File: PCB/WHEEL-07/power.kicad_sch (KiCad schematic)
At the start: 21 parts, among them IC2 LDO40LPU50RY, IC3 MP2332HGTL-P, Q1 AO3401A

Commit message: Changed connectors setup
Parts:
- C14: footprint Capacitor_SMD:C_0201_0603Metric -> Capacitor_SMD:C_0603_1608Metric
- C15, C21, C22: footprint Capacitor_SMD:C_0402_1005Metric -> Capacitor_SMD:C_0402_1005Metric_Pad0.74x0.62mm_HandSolder
- R10, R11, R19, R7, R8, R9: footprint Resistor_SMD:R_0402_1005Metric -> Resistor_SMD:R_0402_1005Metric_Pad0.72x0.64mm_HandSolder
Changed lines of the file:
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@@
     (property "Reference" "R9" (id 0) (at 204.47 57.785 90))
     (property "Value" "20k" (id 1) (at 204.47 55.88 90))
-    (property "Footprint" "Resistor_SMD:R_0402_1005Metric" (id 2) (at 204.47 53.34 0)
+    (property "Footprint" "Resistor_SMD:R_0402_1005Metric_Pad0.72x0.64mm_HandSolder" (id 2) (at 204.47 53.34 0)
       (effects (font (size 1.27 1.27)) hide)
     )
@@
       (effects (font (size 1.27 1.27)) (justify left))
     )
-    (property "Footprint" "Resistor_SMD:R_0402_1005Metric" (id 2) (at 48.26 118.745 0)
+    (property "Footprint" "Resistor_SMD:R_0402_1005Metric_Pad0.72x0.64mm_HandSolder" (id 2) (at 48.26 118.745 0)
       (effects (font (size 1.27 1.27)) hide)
     )
@@
     (property "Reference" "R8" (id 0) (at 203.2 39.37 90))
     (property "Value" "20" (id 1) (at 203.2 41.91 90))
-    (property "Footprint" "Resistor_SMD:R_0402_1005Metric" (id 2) (at 203.2 45.72 0)
+    (property "Footprint" "Resistor_SMD:R_0402_1005Metric_Pad0.72x0.64mm_HandSolder" (id 2) (at 203.2 45.72 0)
       (effects (font (size 1.27 1.27)) hide)
     )
@@
     (property "Reference" "R11" (id 0) (at 217.17 58.42 90))
     (property "Value" "40.2k" (id 1) (at 217.17 55.88 90))
-    (property "Footprint" "Resistor_SMD:R_0402_1005Metric" (id 2) (at 217.17 53.34 0)
+    (property "Footprint" "Resistor_SMD:R_0402_1005Metric_Pad0.72x0.64mm_HandSolder" (id 2) (at 217.17 53.34 0)
       (effects (font (size 1.27 1.27)) hide)
     )
@@
       (effects (font (size 1.27 1.27)) (justify left))
     )
-    (property "Footprint" "Capacitor_SMD:C_0402_1005Metric" (id 2) (at 227.965 45.085 0)
+    (property "Footprint" "Capacitor_SMD:C_0402_1005Metric_Pad0.74x0.62mm_HandSolder" (id 2) (at 227.965 45.085 0)
       (effects (font (size 1.27 1.27)) hide)
     )
@@
     (property "Reference" "R7" (id 0) (at 151.765 52.07 90))
     (property "Value" "200k" (id 1) (at 150.495 53.975 90))
-    (property "Footprint" "Resistor_SMD:R_0402_1005Metric" (id 2) (at 153.035 49.53 0)
+    (property "Footprint" "Resistor_SMD:R_0402_1005Metric_Pad0.72x0.64mm_HandSolder" (id 2) (at 153.035 49.53 0)
       (effects (font (size 1.27 1.27)) hide)
     )
@@
       (effects (font (size 1.27 1.27)) (justify left))
     )
-    (property "Footprint" "Resistor_SMD:R_0402_1005Metric" (id 2) (at 209.55 63.5 0)
+    (property "Footprint" "Resistor_SMD:R_0402_1005Metric_Pad0.72x0.64mm_HandSolder" (id 2) (at 209.55 63.5 0)
       (effects (font (size 1.27 1.27)) hide)
     )
@@
       (effects (font (size 1.27 1.27)) (justify left))
     )
-    (property "Footprint" "Capacitor_SMD:C_0402_1005Metric" (id 2) (at 237.49 45.085 0)
+    (property "Footprint" "Capacitor_SMD:C_0402_1005Metric_Pad0.74x0.62mm_HandSolder" (id 2) (at 237.49 45.085 0)
       (effects (font (size 1.27 1.27)) hide)
     )
@@
       (effects (font (size 1.27 1.27)) (justify left))
     )
-    (property "Footprint" "Capacitor_SMD:C_0201_0603Metric" (id 2) (at 80.645 46.355 0)
+    (property "Footprint" "Capacitor_SMD:C_0603_1608Metric" (id 2) (at 80.645 46.355 0)
       (effects (font (size 1.27 1.27)) hide)
     )
@@
       (effects (font (size 1.27 1.27)) (justify left))
     )
-    (property "Footprint" "Capacitor_SMD:C_0402_1005Metric" (id 2) (at 155.575 41.91 0)
-      (effects (font (size 1.27 1.27)) hide)
-    )
+    (property "Footprint" "Capacitor_SMD:C_0402_1005Metric_Pad0.74x0.62mm_HandSolder" (id 2) (at 155.575 41.91 0)
+      (effects (font (size 1.27 1.27)) hide)
+    )

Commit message: Finished layout
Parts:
- removed R19: 100, Resistor_SMD:R_0402_1005Metric_Pad0.72x0.64mm_HandSolder, symbol Device:R_Small
- C15: footprint Capacitor_SMD:C_0402_1005Metric_Pad0.74x0.62mm_HandSolder -> Capacitor_SMD:C_0805_2012Metric
- C16, C17, C18, C19, C20: footprint (none) -> Capacitor_SMD:C_0402_1005Metric_Pad0.74x0.62mm_HandSolder
- L2: footprint (none) -> Inductor_SMD:L_Vishay_IHLP-1616
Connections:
- net GND: now also Q1.1 (G)
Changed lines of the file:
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@@
   (junction (at 222.25 53.34) (diameter 0) (color 0 0 0 0)
+  )
+  (junction (at 65.405 107.315) (diameter 0) (color 0 0 0 0)
   )
   (junction (at 149.225 45.72) (diameter 0) (color 0 0 0 0)
@@
     (stroke (width 0) (type default) (color 0 0 0 0))
   )
-  (wire (pts (xy 48.26 121.285) (xy 48.26 122.555))
-    (stroke (width 0) (type default) (color 0 0 0 0))
-  )
   (wire (pts (xy 57.785 60.325) (xy 57.785 61.595))
     (stroke (width 0) (type default) (color 0 0 0 0))
@@
     (stroke (width 0) (type default) (color 0 0 0 0))
   )
-  (wire (pts (xy 64.135 107.315) (xy 66.04 107.315))
+  (wire (pts (xy 64.135 107.315) (xy 65.405 107.315))
     (stroke (width 0) (type default) (color 0 0 0 0))
   )
@@
     (stroke (width 0) (type default) (color 0 0 0 0))
   )
+  (wire (pts (xy 65.405 106.045) (xy 65.405 107.315))
+    (stroke (width 0) (type default) (color 0 0 0 0))
+  )
   (wire (pts (xy 237.49 49.53) (xy 240.665 49.53))
     (stroke (width 0) (type default) (color 0 0 0 0))
@@
   )
   (wire (pts (xy 170.18 59.69) (xy 172.085 59.69))
+    (stroke (width 0) (type default) (color 0 0 0 0))
+  )
+  (wire (pts (xy 65.405 107.315) (xy 66.04 107.315))
     (stroke (width 0) (type default) (color 0 0 0 0))
   )
@@
       (effects (font (size 1.27 1.27)) (justify left))
     )
-    (property "Footprint" "" (id 2) (at 166.116 41.91 0)
+    (property "Footprint" "Capacitor_SMD:C_0402_1005Metric_Pad0.74x0.62mm_HandSolder" (id 2) (at 166.116 41.91 0)
       (effects (font (size 1.27 1.27)) hide)
     )
@@
     (pin "2")
   )
-  (symbol (lib_id "Device:R_Small") (at 48.26 118.745 0) (unit 1)
-    (in_bom yes) (on_board yes) (fields_autoplaced)
-    (property "Reference" "R19" (id 0) (at 50.165 117.4749 0)
-      (effects (font (size 1.27 1.27)) (justify left))
-    )
-    (property "Value" "100" (id 1) (at 50.165 120.0149 0)
-      (effects (font (size 1.27 1.27)) (justify left))
-    )
-    (property "Footprint" "Resistor_SMD:R_0402_1005Metric_Pad0.72x0.64mm_HandSolder" (id 2) (at 48.26 118.745 0)
-      (effects (font (size 1.27 1.27)) hide)
-    )
-    (property "Datasheet" "~" (id 3) (at 48.26 118.745 0)
-      (effects (font (size 1.27 1.27)) hide)
-    )
-    (pin "1")
-    (pin "2")
-  )
   (symbol (lib_id "WHEEL_07:LDO40LPU50RY") (at 40.005 37.465 0) (unit 1)
     (in_bom yes) (on_board yes) (fields_autoplaced)
@@
     (pin "1")
   )
-  (symbol (lib_id "power:GND") (at 48.26 122.555 0) (unit 1)
-    (in_bom yes) (on_board yes) (fields_autoplaced)
-    (property "Reference" "#PWR0168" (id 0) (at 48.26 128.905 0)
-      (effects (font (size 1.27 1.27)) hide)
-    )
-    (property "Value" "GND" (id 1) (at 48.26 127 0))
-    (property "Footprint" "" (id 2) (at 48.26 122.555 0)
-      (effects (font (size 1.27 1.27)) hide)
-    )
-    (property "Datasheet" "" (id 3) (at 48.26 122.555 0)
+  (symbol (lib_id "power:GND") (at 48.26 116.205 0) (unit 1)
+    (in_bom yes) (on_board yes) (fields_autoplaced)
+    (property "Reference" "#PWR0168" (id 0) (at 48.26 122.555 0)
+      (effects (font (size 1.27 1.27)) hide)
+    )
+    (property "Value" "GND" (id 1) (at 48.26 120.65 0))
+    (property "Footprint" "" (id 2) (at 48.26 116.205 0)
+      (effects (font (size 1.27 1.27)) hide)
+    )
+    (property "Datasheet" "" (id 3) (at 48.26 116.205 0)
       (effects (font (size 1.27 1.27)) hide)
     )
@@
     (property "Reference" "C20" (id 0) (at 217.17 67.945 90))
     (property "Value" "10pF" (id 1) (at 217.17 69.85 90))
-    (property "Footprint" "" (id 2) (at 217.17 64.77 0)
+    (property "Footprint" "Capacitor_SMD:C_0402_1005Metric_Pad0.74x0.62mm_HandSolder" (id 2) (at 217.17 64.77 0)
       (effects (font (size 1.27 1.27)) hide)
     )
@@
       (effects (font (size 1.27 1.27)) (justify right))
     )
-    (property "Footprint" "" (id 2) (at 162.56 57.15 0)
+    (property "Footprint" "Capacitor_SMD:C_0402_1005Metric_Pad0.74x0.62mm_HandSolder" (id 2) (at 162.56 57.15 0)
       (effects (font (size 1.27 1.27)) hide)
     )
@@
       (effects (font (size 1.27 1.27)) (justify right))
     )
-    (property "Footprint" "" (id 2) (at 170.18 63.5 0)
+    (property "Footprint" "Capacitor_SMD:C_0402_1005Metric_Pad0.74x0.62mm_HandSolder" (id 2) (at 170.18 63.5 0)
       (effects (font (size 1.27 1.27)) hide)
     )
@@
     (property "Reference" "L2" (id 0) (at 220.345 44.45 90))
     (property "Value" "2.2uH" (id 1) (at 220.345 46.99 90))
-    (property "Footprint" "" (id 2) (at 220.345 49.53 0)
+    (property "Footprint" "Inductor_SMD:L_Vishay_IHLP-1616" (id 2) (at 220.345 49.53 0)
       (effects (font (size 1.27 1.27)) hide)
     )
@@
     (pin "1")
   )
+  (symbol (lib_id "power:PWR_FLAG") (at 65.405 106.045 0) (unit 1)
+    (in_bom yes) (on_board yes)
+    (property "Reference" "#FLG0106" (id 0) (at 65.405 104.14 0)
+      (effects (font (size 1.27 1.27)) hide)
+    )
+    (property "Value" "PWR_FLAG" (id 1) (at 65.405 98.425 90))
+    (property "Footprint" "" (id 2) (at 65.405 106.045 0)
+      (effects (font (size 1.27 1.27)) hide)
+    )
+    (property "Datasheet" "~" (id 3) (at 65.405 106.045 0)
+      (effects (font (size 1.27 1.27)) hide)
+    )
+    (pin "1")
+  )
   (symbol (lib_id "Device:C_Small") (at 212.09 45.72 90) (unit 1)
     (in_bom yes) (on_board yes) (fields_autoplaced)
     (property "Reference" "C19" (id 0) (at 212.0963 39.37 90))
     (property "Value" "1uF" (id 1) (at 212.0963 41.91 90))
-    (property "Footprint" "" (id 2) (at 212.09 45.72 0)
+    (property "Footprint" "Capacitor_SMD:C_0402_1005Metric_Pad0.74x0.62mm_HandSolder" (id 2) (at 212.09 45.72 0)
       (effects (font (size 1.27 1.27)) hide)
     )
@@
       (effects (font (size 1.27 1.27)) (justify left))
     )
-    (property "Footprint" "Capacitor_SMD:C_0402_1005Metric_Pad0.74x0.62mm_HandSolder" (id 2) (at 155.575 41.91 0)
-      (effects (font (size 1.27 1.27)) hide)
-    )
+    (property "Footprint" "Capacitor_SMD:C_0805_2012Metric" (id 2) (at 155.575 41.91 0)
+      (effects (font (size 1.27 1.27)) hide)
+    )

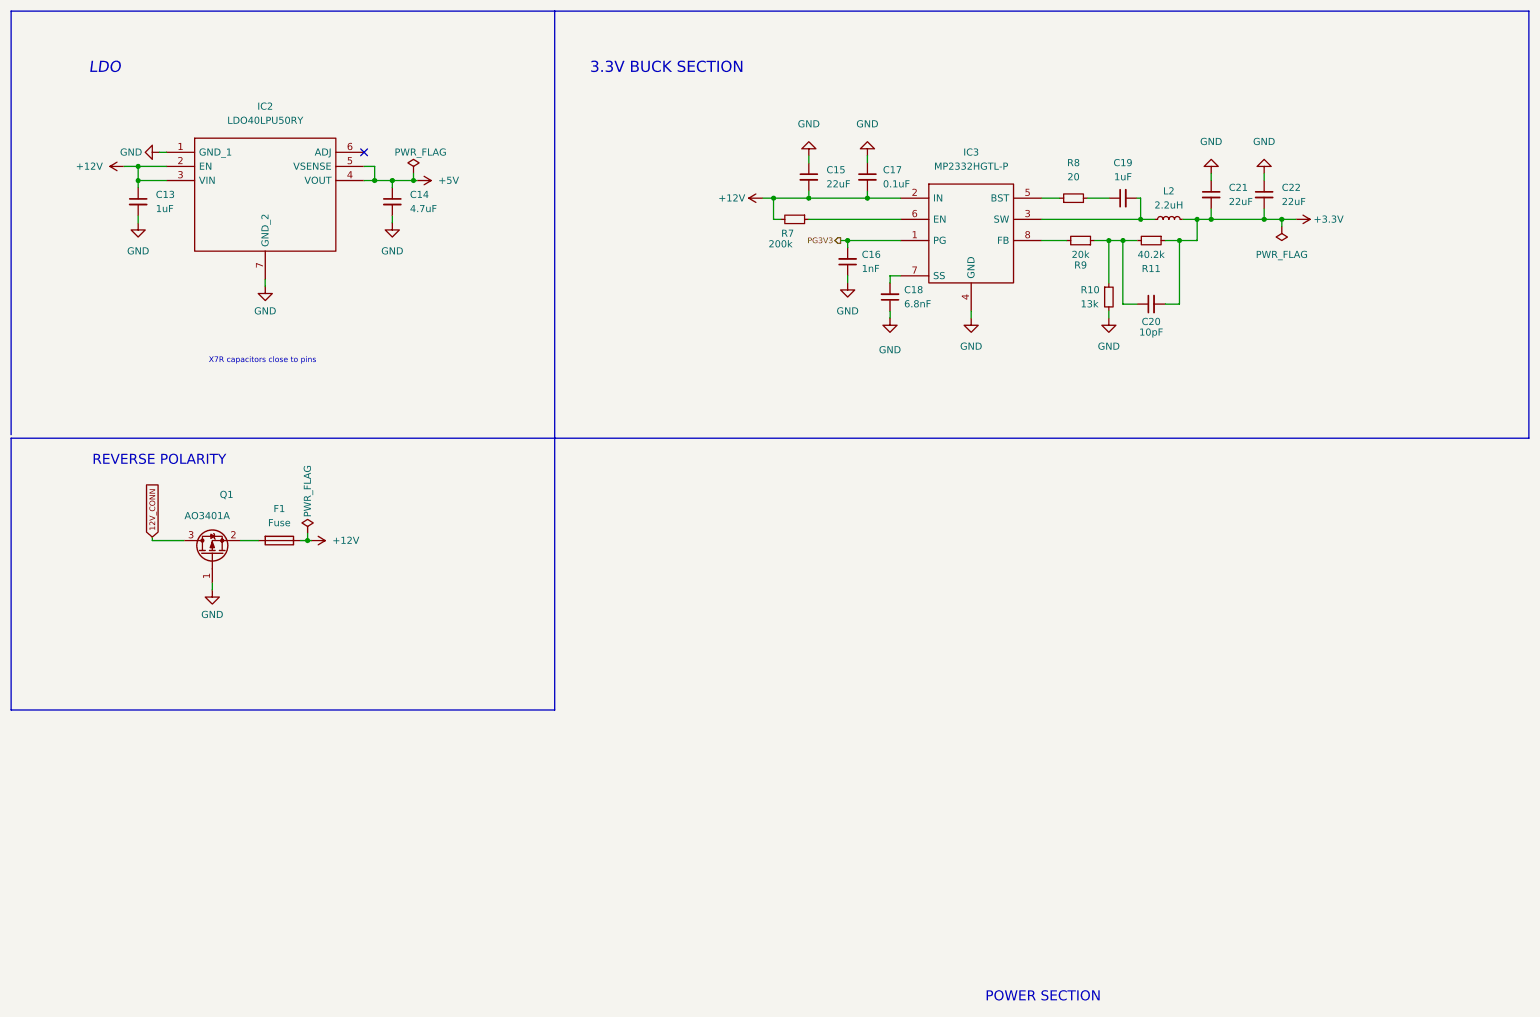
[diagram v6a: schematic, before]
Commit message: Changed power supply section for 2 x LDO40
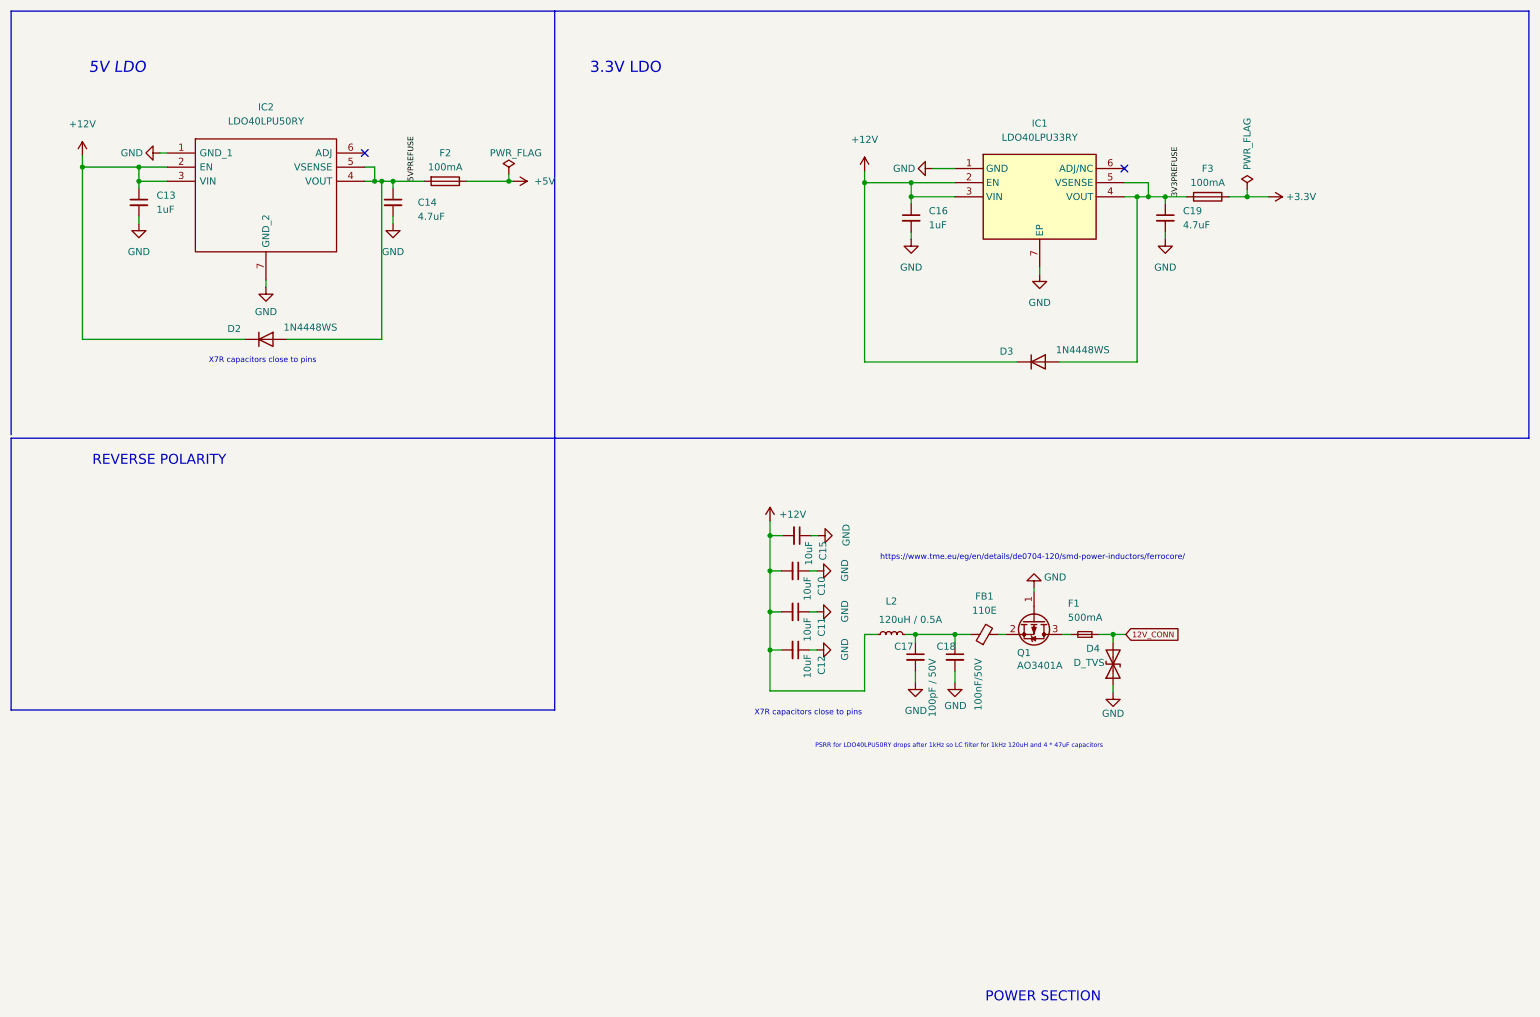
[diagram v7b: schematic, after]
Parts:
- removed C20: 10pF, Capacitor_SMD:C_0402_1005Metric_Pad0.74x0.62mm_HandSolder, symbol Device:C_Small
- removed C21, C22: 22uF, Capacitor_SMD:C_0402_1005Metric_Pad0.74x0.62mm_HandSolder, symbol Device:C_Small
- removed F1: Fuse, Fuse:Fuse_0805_2012Metric, symbol Device:Fuse
- removed IC3: MP2332HGTL-P, WHEEL_07_LIBRARY_LOADER:SOTFL50P160X60-8N, symbol WHEEL_07_LIBRARY_LOADER:MP2332HGTL-P
- removed R10: 13k, Resistor_SMD:R_0402_1005Metric_Pad0.72x0.64mm_HandSolder, symbol Device:R_Small
- removed R11: 40.2k, Resistor_SMD:R_0402_1005Metric_Pad0.72x0.64mm_HandSolder, symbol Device:R_Small
- removed R7: 200k, Resistor_SMD:R_0402_1005Metric_Pad0.72x0.64mm_HandSolder, symbol Device:R_Small
- removed R8: 20, Resistor_SMD:R_0402_1005Metric_Pad0.72x0.64mm_HandSolder, symbol Device:R_Small
- removed R9: 20k, Resistor_SMD:R_0402_1005Metric_Pad0.72x0.64mm_HandSolder, symbol Device:R_Small
- added C10, C11, C12: 10uF, Capacitor_SMD:C_1206_3216Metric, symbol Device:C_Small
- added D2, D3: 1N4448WS, Diode_SMD:D_SOD-323, symbol Diode:1N4448WS
- added D4: D_TVS, Diode_SMD:D_SMA, symbol Device:D_TVS
- added F1: 500mA, Fuse:Fuse_0805_2012Metric, symbol Device:Fuse_Small
- added F2, F3: 100mA, Fuse:Fuse_0805_2012Metric, symbol Device:Fuse
- added FB1: 110E, LED_SMD:LED_0805_2012Metric, symbol Device:FerriteBead_Small
- added IC1: LDO40LPU33RY, PDMS_Additional:SON95P300X300X90-7N-D, symbol pdms_additional:LDO40LPU33RY
- C15: value 22uF -> 10uF; footprint Capacitor_SMD:C_0805_2012Metric -> Capacitor_SMD:C_1206_3216Metric
- C16: value 1nF -> 1uF; footprint Capacitor_SMD:C_0402_1005Metric_Pad0.74x0.62mm_HandSolder -> Capacitor_SMD:C_0805_2012Metric
- C17: value 0.1uF -> 100pF / 50V; footprint Capacitor_SMD:C_0402_1005Metric_Pad0.74x0.62mm_HandSolder -> Capacitor_SMD:C_0402_1005Metric
- C18: value 6.8nF -> 100nF/50V; footprint Capacitor_SMD:C_0402_1005Metric_Pad0.74x0.62mm_HandSolder -> Capacitor_SMD:C_0402_1005Metric
- C19: value 1uF -> 4.7uF; footprint Capacitor_SMD:C_0402_1005Metric_Pad0.74x0.62mm_HandSolder -> Capacitor_SMD:C_0603_1608Metric
- L2: value 2.2uH -> 120uH / 0.5A; footprint Inductor_SMD:L_Vishay_IHLP-1616 -> Inductor_SMD:L_7.3x7.3_H4.5
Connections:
- net PG3V3 is gone; now on net GND: C16.2
- net +12V: now also C16.1, L2.1, C10.2, C11.2, C12.2, D2.1 (K), D3.1 (K), IC1.2 (EN), IC1.3 (VIN); no longer C17.2
- net +3.3V: now also F3.1; no longer L2.2
- net +5V: now also F2.1; no longer C14.1, IC2.4 (VOUT), IC2.5 (VSENSE)
- net 12V_CONN: now also D4.2 (A2), F1.1; no longer Q1.3 (D)
- net GND: now also C17.2, C18.2, C19.2, C10.1, C11.1, C12.1, D4.1 (A1), IC1.1 (GND), IC1.7 (EP); no longer C16.1, C17.1, C18.1
- net 3V3PREFUSE: now reaches C19.1
- net 3V3PREFUSE: now also D3.2 (A), F3.2, IC1.4 (VOUT), IC1.5 (VSENSE)
- net at Q1.2 (S): now also FB1.2
- new net: C17.1, C18.1, FB1.1, L2.2
- new net: F1.2, Q1.3 (D)
- new net 5VPREFUSE: C14.1, D2.2 (A), F2.2, IC2.4 (VOUT), IC2.5 (VSENSE)
- no-connect marks 1 -> 2
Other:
- note added: "3.3V LDO"
- note added: "5V LDO"
- note added: "PSRR for LDO40LPU50RY drops after 1kHz so LC filter for 1kHz 120uH and 4 * 47uF capacitors"
- note added: "https://www.tme.eu/eg/en/details/de0704-120/smd-power-inductors/ferrocore/"
- note removed: "3.3V BUCK SECTION"
- note removed: "LDO"
